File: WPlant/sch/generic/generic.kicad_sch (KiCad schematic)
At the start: 20 parts, among them J1 PROG/JTAG, U1 SIWG917Y121MGABAR

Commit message: Added Generic changes
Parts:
- added BUZ1: HNR-1407PA7.5, easyeda2kicad:BUZ-TH_BD14.0-P7.60-D0.8-L, symbol easyeda2kicad:HNR-1407PA7.5
- added C30: 0.1, symbol Device:C
- added C31: C, symbol Device:C
- added R19: 33, symbol Device:R
- added U5: TC4427AEOA713, easyeda2kicad:SOIC-8_L4.9-W3.9-P1.27-LS6.0-BL, symbol easyeda2kicad:TC4427AEOA713
- added U7: NC7S02P5, easyeda2kicad:SC-70-5_L2.1-W1.3-P0.65-LS2.1-BL, symbol easyeda2kicad:NC7S02P5
- added X1: SIT1552AI-JE-DCC-32.768D, easyeda2kicad:OSC-SMD_4P-L1.5-W0.8-BL, symbol easyeda2kicad:SIT1552AI-JE-DCC-32.768D
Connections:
- net +3.3V: now also C30.2, X1.3 (VDD)
- net GND: now also C30.1, X1.1 (GND), X1.4 (GND)
- net at U1.29 (UULP_VBAT_GPIO_3): now also R19.2
- net EN9: now reaches U1.7 (ULP_GPIO_7)
- new net: BUZ1.1, C31.2
- new net: BUZ1.2, U5.5 (~{OUTB})
- new net: R19.1, X1.2 (CLK_OUT)
- new net: U5.2 (INA), U7.1 (A)
- new net: U5.4 (INB), U7.4 (Y)
- new net: C31.1, U5.7 (~{OUTA})
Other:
- added sheet Power (power.kicad_sch)

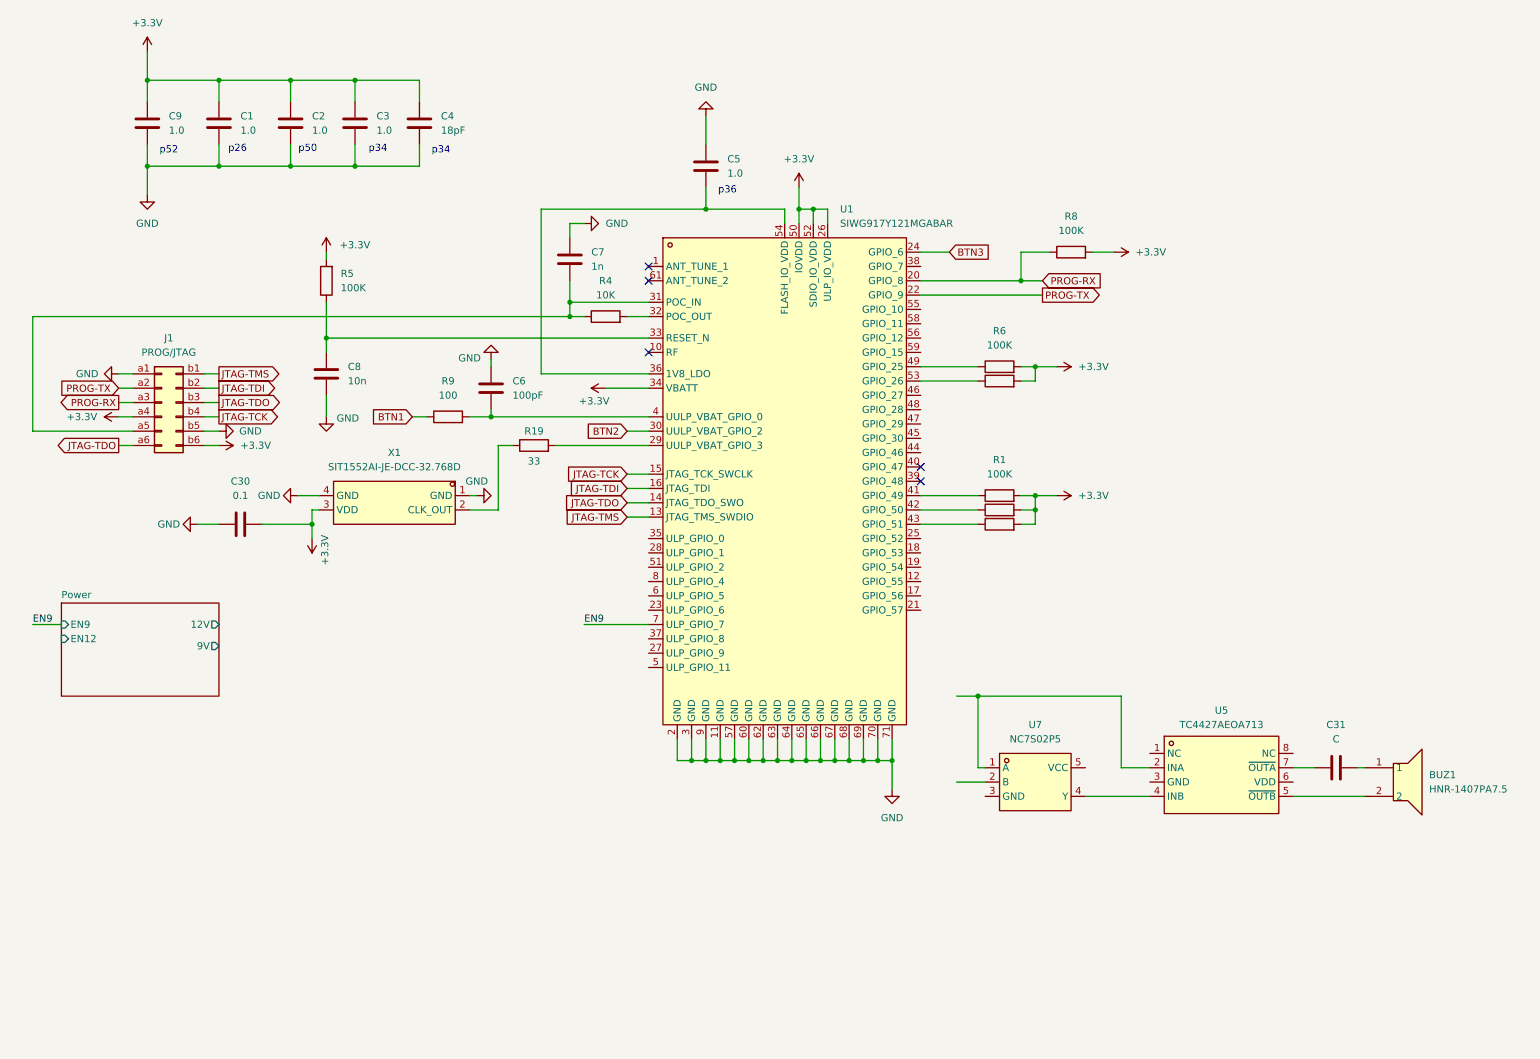
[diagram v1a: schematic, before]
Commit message: Generic schematic almost done
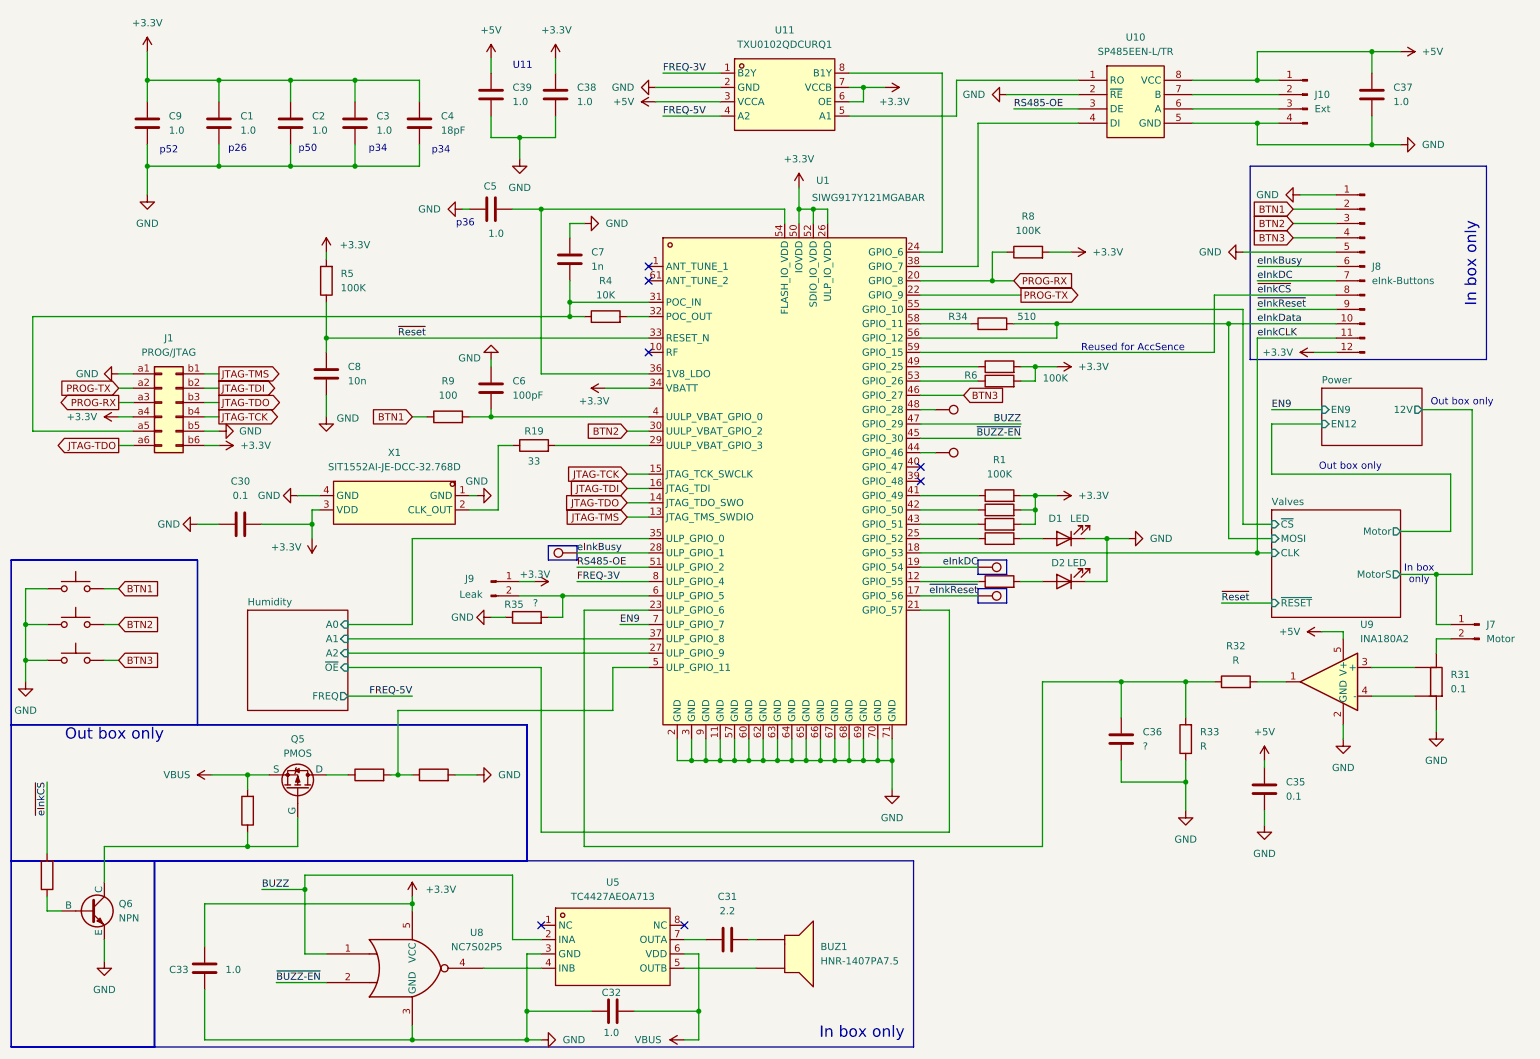
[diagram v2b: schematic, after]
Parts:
- removed U7: NC7S02P5, easyeda2kicad:SC-70-5_L2.1-W1.3-P0.65-LS2.1-BL, symbol easyeda2kicad:NC7S02P5
- added C32, C33, C37, C38, C39: 1.0, symbol Device:C
- added C35: 0.1, symbol Device:C
- added C36: ?, symbol Device:C
- added D1, D2: LED, symbol Device:LED
- added J10: Ext, symbol Connector:Conn_01x04_Pin
- added J7: Motor, symbol Connector:Conn_01x02_Pin
- added J8: eInk-Buttons, symbol Connector:Conn_01x12_Pin
- added J9: Leak, symbol Connector:Conn_01x02_Pin
- added Q5: PMOS, symbol Simulation_SPICE:PMOS
- added Q6: NPN, symbol Simulation_SPICE:NPN
- added R21, R22, R36, R37, R38, R39: 100K, symbol Device:R
- added R31: 0.1, symbol Device:R_Shunt
- added R32, R33: R, symbol Device:R
- added R34: 510, symbol Device:R
- added R35: ?, symbol Device:R
- added SW1, SW2, SW3: SW_Push, symbol Switch:SW_Push
- added TP1, TP2, TP3, TP4, TP5: TestPoint, symbol Connector:TestPoint
- added U10: SP485EEN-L/TR, easyeda2kicad:SOIC-8_L5.0-W4.0-P1.27-LS6.0-BL, symbol EasyEDA:SP485EEN-L_TR
- added U11: TXU0102QDCURQ1, easyeda2kicad:VSSOP-8_L2.3-W2.0-P0.50-LS3.1-BL, symbol EasyEDA:TXU0102QDCURQ1
- added U8: NC7S02P5, easyeda2kicad:SC-70-5_L2.1-W1.3-P0.65-LS2.1-BL, symbol 74xGxx:74LVC1G02
- added U9: INA180A2, Package_TO_SOT_SMD:SOT-23-5, symbol Amplifier_Current:INA180A2
- C31: value C -> 2.2
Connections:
- net +3.3V: now also C33.2, C38.1, J8.12 (Pin_12), J9.1 (Pin_1), U11.6 (OE), U11.7 (VCCB), U8.5 (VCC)
- net BTN1: now also J8.2 (Pin_2), SW1.2
- net BTN2: now also J8.3 (Pin_3), SW2.2
- net BTN3: now also U1.46 (GPIO_27), J8.4 (Pin_4), SW3.2; no longer U1.24 (GPIO_6)
- net GND: now also U5.3 (GND), C32.1, C33.1, C35.2, C36.2, C37.2, C38.2, C39.2, D1.1 (K), D2.1 (K), J10.4 (Pin_4), J8.1 (Pin_1), J8.5 (Pin_5), Q6.3 (E), R31.4, R33.1, R35.1, R37.2, SW1.1, SW2.1, SW3.1, U10.2 (~{RE}), U10.5 (GND), U11.2 (GND), U8.3 (GND), U9.2 (GND)
- net Power/12V: now also J7.1 (Pin_1)
- net ~{Reset}: now reaches C8.1, R5.1, U1.33 (RESET_N)
- net at U1.12 (GPIO_55): now also R22.1
- net ~{eInkReset}: now reaches U1.17 (GPIO_56)
- net ~{eInkReset}: now also J8.9 (Pin_9), TP4.1
- net eInkCLK: now reaches U1.18 (GPIO_53)
- net eInkCLK: now also J8.11 (Pin_11)
- net eInkDC: now reaches U1.19 (GPIO_54)
- net eInkDC: now also J8.7 (Pin_7), TP3.1
- net Humidity/~{OE}: now reaches U1.21 (GPIO_57)
- net at U1.23 (ULP_GPIO_6): now also C36.1, R32.1, R33.2
- net at U1.25 (GPIO_52): now also R21.1
- net Humidity/A2: now reaches U1.27 (ULP_GPIO_9)
- net eInkBusy: now reaches U1.28 (ULP_GPIO_1)
- net eInkBusy: now also J8.6 (Pin_6), TP5.1
- net Humidity/A0: now reaches U1.35 (ULP_GPIO_0)
- net Humidity/A1: now reaches U1.37 (ULP_GPIO_8)
- net at U1.38 (GPIO_7): now also U10.4 (DI)
- net at U1.44 (GPIO_46): now also TP1.1
- net ~{BUZZ-EN}: now reaches U1.45 (GPIO_30)
- net ~{BUZZ-EN}: now also U8.2
- net BUZZ: now reaches U1.47 (GPIO_29)
- net BUZZ: now also U5.2 (INA), U8.1
- net at U1.48 (GPIO_28): now also TP2.1
- net at U1.5 (ULP_GPIO_11): now also R36.2, R37.1
- net RS485-OE: now reaches U1.51 (ULP_GPIO_2)
- net RS485-OE: now also U10.3 (DE)
- net Valves/~{CS}: now reaches U1.55 (GPIO_10)
- net eInkData: now reaches U1.56 (GPIO_12)
- net eInkData: now also J8.10 (Pin_10), R34.2
- net at U1.58 (GPIO_11): now also R34.1
- net ~{eInkCS}: now reaches U1.59 (GPIO_15)
- net ~{eInkCS}: now also J8.8 (Pin_8), R39.2
- net at U1.6 (ULP_GPIO_5): now also J9.2 (Pin_2), R35.2
- net FREQ-3V: now reaches U1.8 (ULP_GPIO_4)
- net FREQ-3V: now also U11.1 (B2Y)
- net at U5.4 (INB): now also U8.4
- net VBUS: now reaches U5.6 (VDD)
- net VBUS: now also C32.2, Q5.3 (S), R38.2
- new net: J10.2 (Pin_2), U10.7 (B)
- new net: J10.3 (Pin_3), U10.6 (A)
- new net: D2.2 (A), R22.2
- new net: Q5.1 (D), R36.1
- new net: Q5.2 (G), Q6.1 (C), R38.1
- new net: J7.2 (Pin_2), R31.1
- new net: D1.2 (A), R21.2
- new net: U10.1 (RO), U11.5 (A1)
- new net: U1.24 (GPIO_6), U11.8 (B1Y)
- new net: Q6.2 (B), R39.1
- new net: R31.2, U9.3 (+)
- new net: R31.3, U9.4 (-)
- new net: R32.2, U9.1
- new net +5V: C35.1, C37.1, C39.1, J10.1 (Pin_1), U10.8 (VCC), U11.3 (VCCA), U9.5 (V+)
- new net FREQ-5V: U11.4 (A2)
- no-connect marks 5 -> 7
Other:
- added sheet Humidity (humidity.kicad_sch)
- added sheet Valves (valves.kicad_sch)
- sheet Power ports: added none; removed 9V
- note added: "In box only"
- note added: "Out box only"
- note added: "Reused for AccSence"
- note added: "U11"
- company: (none) -> RoboWay
- title: (none) -> Water Plant main module
- moved on the sheet: C31, C5, R8, U5

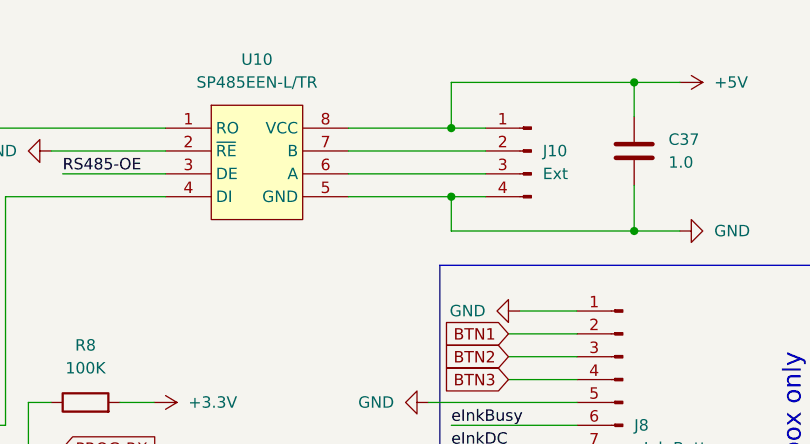
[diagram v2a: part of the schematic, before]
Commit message: Updated Generic WP schematic
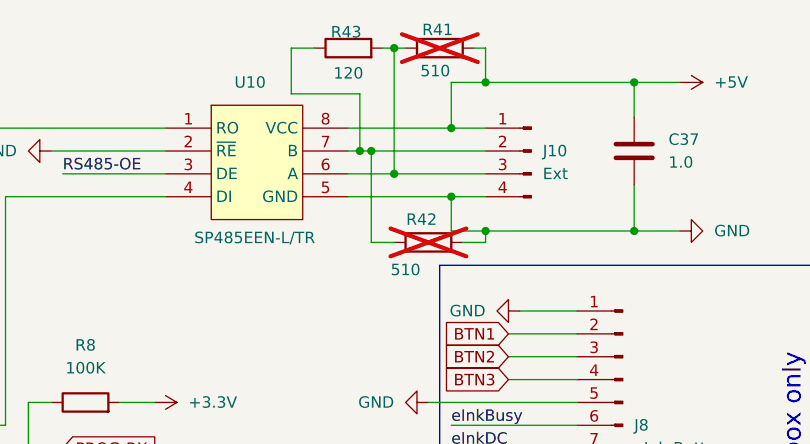
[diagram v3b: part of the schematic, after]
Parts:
- added R41, R42: 510, symbol Device:R
- added R43: 120, symbol Device:R
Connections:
- net +5V: now also R41.2
- net GND: now also R42.2
- net at J10.2 (Pin_2), U10.7 (B): now also R42.1, R43.1
- net at J10.3 (Pin_3), U10.6 (A): now also R41.1, R43.2

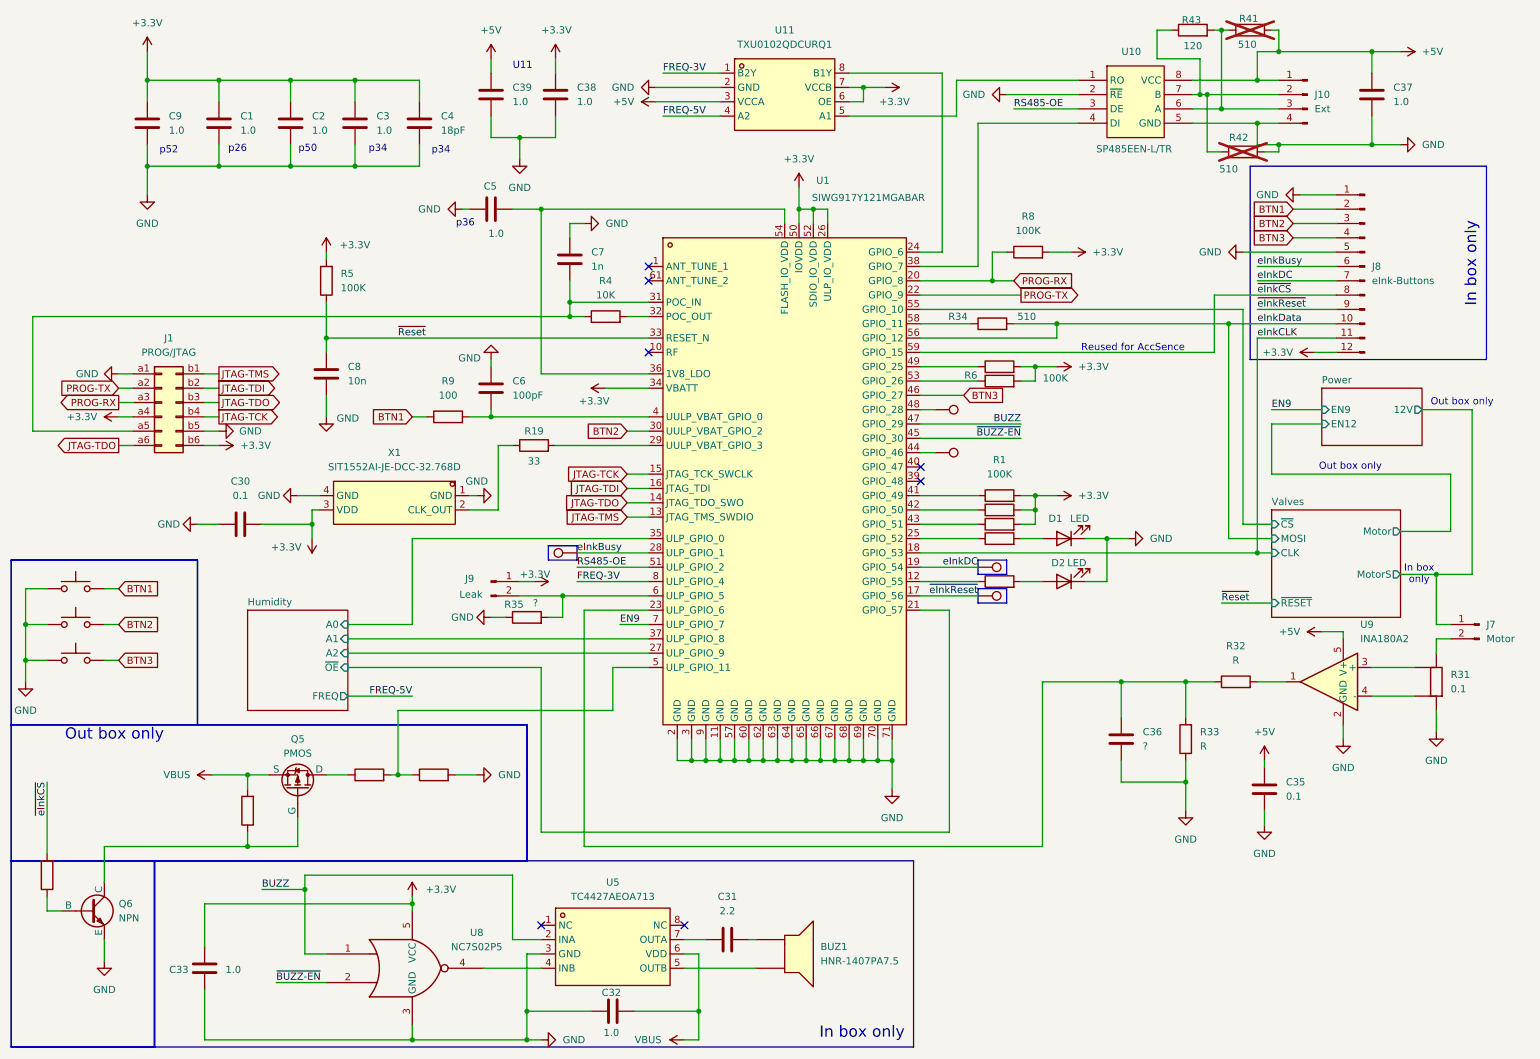
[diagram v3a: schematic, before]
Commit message: Small updates SCH of WP Generic part
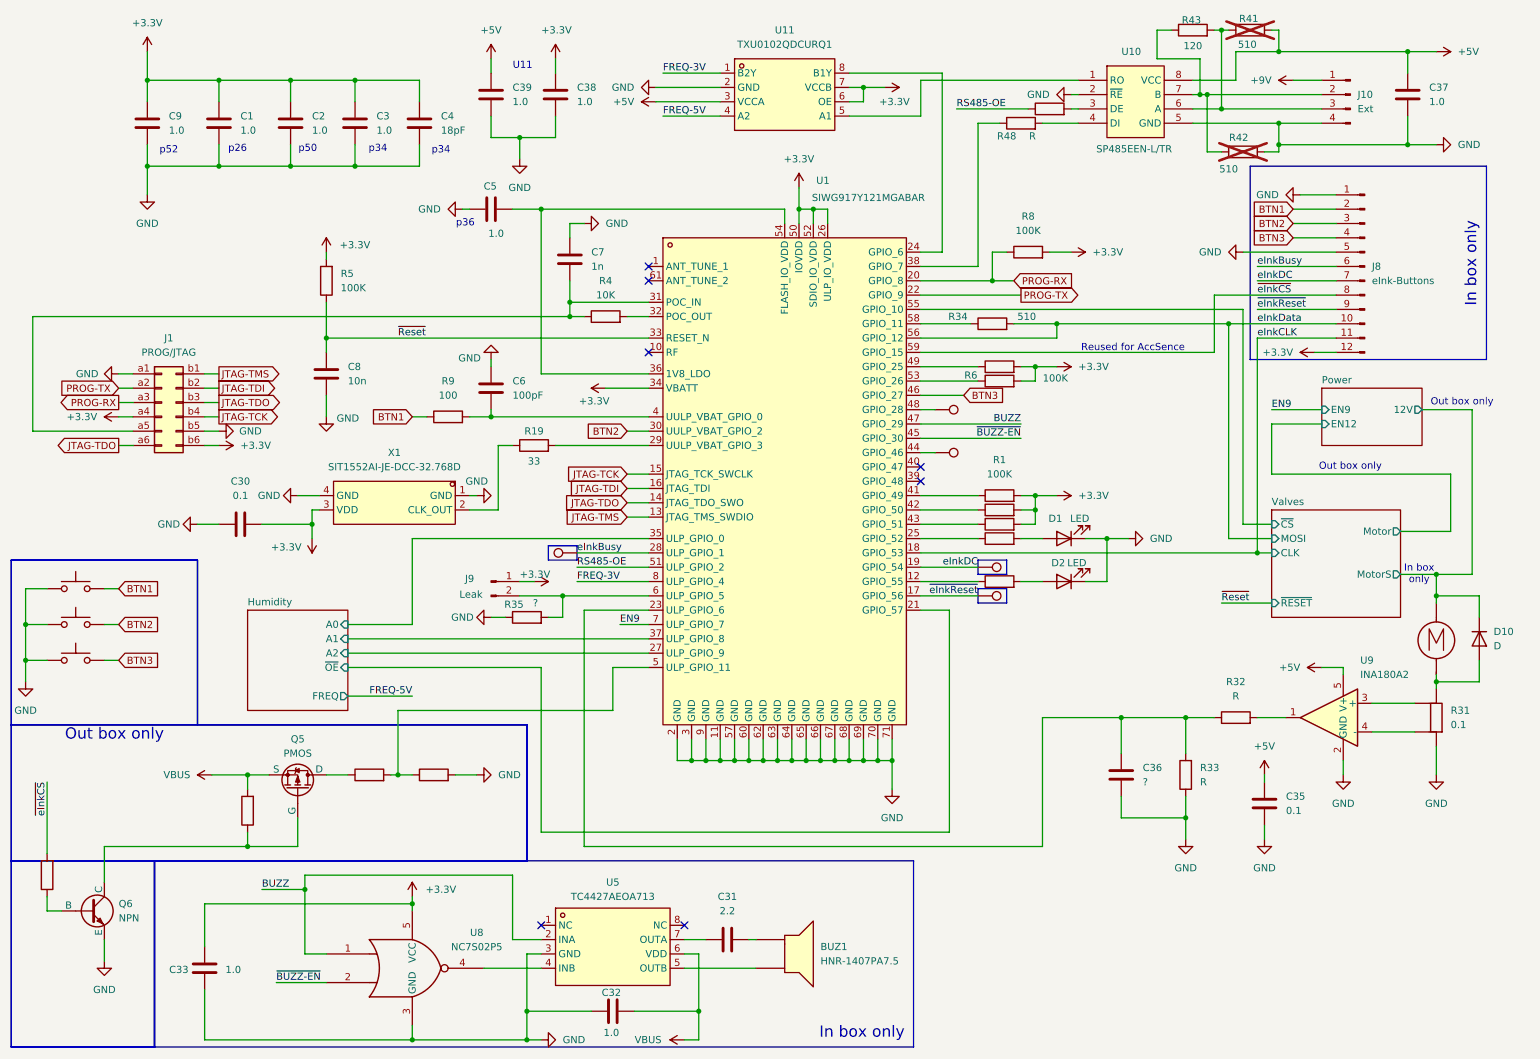
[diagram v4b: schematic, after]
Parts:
- removed J7: Motor, symbol Connector:Conn_01x02_Pin
- added D10: D, symbol Device:D
- added M1: Motor_DC, symbol Motor:Motor_DC
- added R48, R49: R, symbol Device:R
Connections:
- net +5V: no longer J10.1 (Pin_1)
- net Power/12V: now also D10.1 (K), M1.1 (+)
- net RS485-OE: now also R49.1; no longer U10.3 (DE)
- net at R31.1: now also D10.2 (A), M1.2 (-)
- net at U10.4 (DI): now also R48.2; no longer U1.38 (GPIO_7)
- new net: R49.2, U10.3 (DE)
- new net: R48.1, U1.38 (GPIO_7)
- new net +9V: J10.1 (Pin_1)
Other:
- moved on the sheet: C35, C36, C37, J10, R31, R32, R33, U9
